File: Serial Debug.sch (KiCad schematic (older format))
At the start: 19 parts, among them J7 USB_OTG, U9 FT230XQ

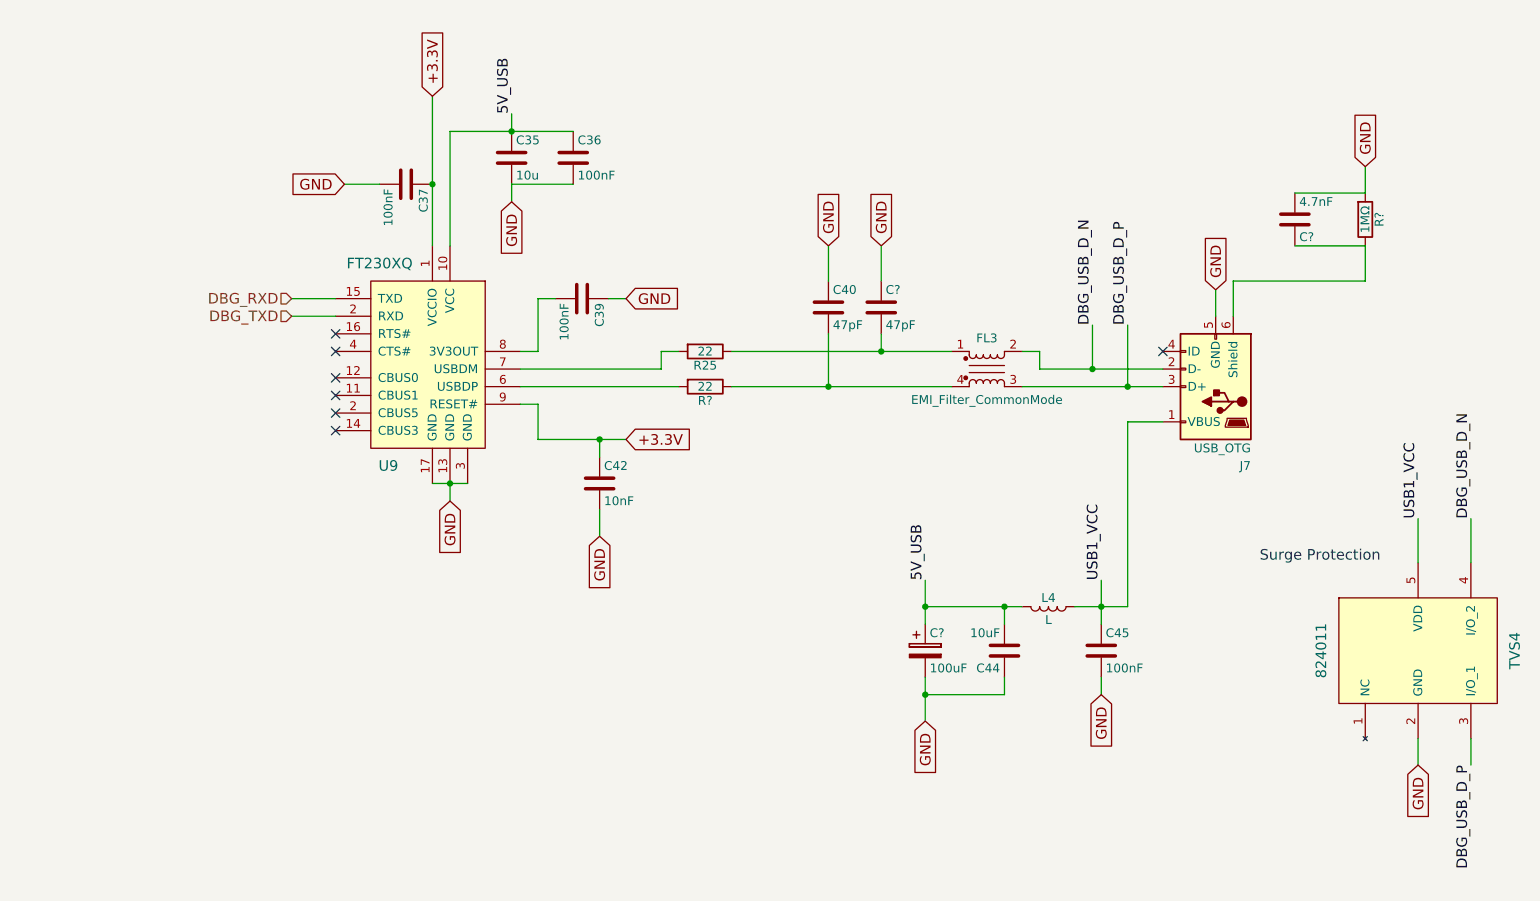
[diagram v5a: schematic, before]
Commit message: part numbers generated;
pcb generation started
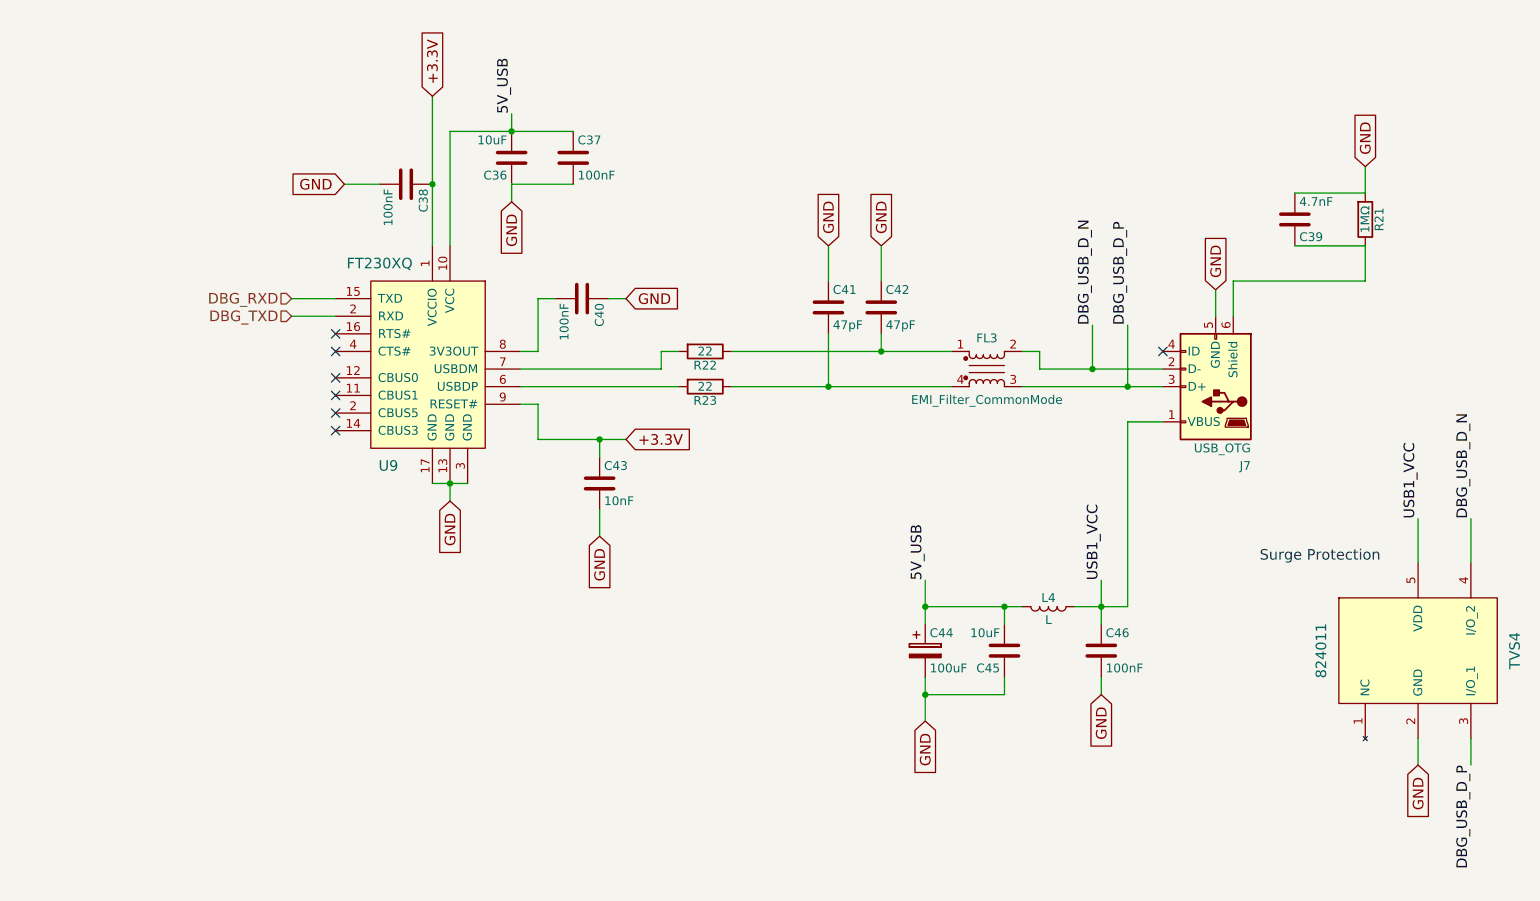
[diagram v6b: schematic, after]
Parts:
- removed C35: 10u, symbol C
- added C36: 10uF, Capacitors_SMD:C_0603_HandSoldering, symbol C
- gave numbers to parts that had none: 5
- renumbered C36 to C37, C37 to C38, C39 to C40, C40 to C41, C42 to C43, C44 to C45, C45 to C46, R25 to R22
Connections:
- net 5V_USB: now also C36.2
- net GND: now also C36.1
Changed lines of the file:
@@
 	3200 3450 3200 3650
 $Comp
-L R R25
+L R R22
 U 1 1 59A2A431
 P 4150 3150
-F 0 "R25" V 4230 3150 50  0000 C CNN
+F 0 "R22" V 4230 3150 50  0000 C CNN
 F 1 "22" V 4150 3150 50  0000 C CNN
 F 2 "Resistors_SMD:R_0603_HandSoldering" V 4080 3150 50  0001 C CNN
@@
 GND
 $Comp
-L C C40
+L C C41
 U 1 1 59A2FC88
 P 4850 2900
-F 0 "C40" H 4875 3000 50  0000 L CNN
+F 0 "C41" H 4875 3000 50  0000 L CNN
 F 1 "47pF" H 4875 2800 50  0000 L CNN
 F 2 "Capacitors_SMD:C_0603_HandSoldering" H 4888 2750 50  0001 C CNN
@@
 Text Label 3050 1800 1    60   ~ 0
 5V_USB
-$Comp
-L C C35
-U 1 1 59A63DF8
-P 3050 2050
-F 0 "C35" H 3075 2150 50  0000 L CNN
-F 1 "10u" H 3075 1950 50  0000 L CNN
-F 2 "" H 3088 1900 50  0001 C CNN
-F 3 "" H 3050 2050 50  0001 C CNN
-	1    3050 2050
-	1    0    0    -1
-$EndComp
 Text GLabel 3050 2300 3    60   Input ~ 0
 GND
@@
 	3900 3150 4000 3150
 $Comp
-L C C44
+L C C45
 U 1 1 59A86400
 P 5850 4850
-F 0 "C44" H 5875 4950 50  0000 L CNN
+F 0 "C45" H 5875 4950 50  0000 L CNN
 F 1 "10uF" H 5875 4750 50  0000 L CNN
 F 2 "Capacitors_SMD:C_0603_HandSoldering" H 5888 4700 30  0001 C CNN
@@
 Connection ~ 5850 4600
 $Comp
-L C C42
+L C C43
 U 1 1 59A67671
 P 3550 3900
-F 0 "C42" H 3575 4000 50  0000 L CNN
+F 0 "C43" H 3575 4000 50  0000 L CNN
 F 1 "10nF" H 3575 3800 50  0000 L CNN
 F 2 "Capacitors_SMD:C_0603_HandSoldering" H 3588 3750 50  0001 C CNN
@@
 $EndComp
 $Comp
-L C C39
+L C C40
 U 1 1 59A67F9E
 P 3450 2850
-F 0 "C39" H 3475 2950 50  0000 L CNN
+F 0 "C40" H 3475 2950 50  0000 L CNN
 F 1 "100nF" H 3475 2750 50  0000 L CNN
 F 2 "Capacitors_SMD:C_0603_HandSoldering" H 3488 2700 30  0001 C CNN
@@
 $EndComp
 $Comp
-L C C45
+L C C46
 U 1 1 59A68788
 P 6400 4850
-F 0 "C45" H 6425 4950 50  0000 L CNN
+F 0 "C46" H 6425 4950 50  0000 L CNN
 F 1 "100nF" H 6425 4750 50  0000 L CNN
 F 2 "Capacitors_SMD:C_0603_HandSoldering" H 6438 4700 30  0001 C CNN
@@
 $EndComp
 $Comp
-L C C36
+L C C37
 U 1 1 59A68F5E
 P 3400 2050
-F 0 "C36" H 3425 2150 50  0000 L CNN
+F 0 "C37" H 3425 2150 50  0000 L CNN
 F 1 "100nF" H 3425 1950 50  0000 L CNN
 F 2 "Capacitors_SMD:C_0603_HandSoldering" H 3438 1900 30  0001 C CNN
@@
 $EndComp
 $Comp
-L C C37
+L C C38
 U 1 1 59A69729
 P 2450 2200
-F 0 "C37" H 2475 2300 50  0000 L CNN
+F 0 "C38" H 2475 2300 50  0000 L CNN
 F 1 "100nF" H 2475 2100 50  0000 L CNN
 F 2 "Capacitors_SMD:C_0603_HandSoldering" H 2488 2050 30  0001 C CNN
@@
 $EndComp
 $Comp
-L R R?
+L R R21
 U 1 1 59AA0F3A
 P 7900 2400
-F 0 "R?" V 7980 2400 50  0000 C CNN
+F 0 "R21" V 7980 2400 50  0000 C CNN
 F 1 "1MΩ" V 7900 2400 50  0000 C CNN
 F 2 "Resistors_SMD:R_0603_HandSoldering" V 7830 2400 50  0001 C CNN
@@
 $EndComp
 $Comp
-L C C?
+L C C39
 U 1 1 59AA0F41
 P 7500 2400
-F 0 "C?" H 7525 2500 50  0000 L CNN
+F 0 "C39" H 7525 2500 50  0000 L CNN
 F 1 "4.7nF" H 7525 2300 50  0000 L CNN
 F 2 "Capacitors_SMD:C_0603_HandSoldering" H 7538 2250 50  0001 C CNN
@@
 	7900 2250 7900 2100
 $Comp
-L R R?
+L R R23
 U 1 1 59A9B327
 P 4150 3350
-F 0 "R?" V 4230 3350 50  0000 C CNN
+F 0 "R23" V 4230 3350 50  0000 C CNN
 F 1 "22" V 4150 3350 50  0000 C CNN
 F 2 "Resistors_SMD:R_0603_HandSoldering" V 4080 3350 50  0001 C CNN
@@
 $EndComp
 $Comp
-L C C?
+L C C42
 U 1 1 59A9B888
 P 5150 2900
-F 0 "C?" H 5175 3000 50  0000 L CNN
+F 0 "C42" H 5175 3000 50  0000 L CNN
 F 1 "47pF" H 5175 2800 50  0000 L CNN
 F 2 "Capacitors_SMD:C_0603_HandSoldering" H 5188 2750 50  0001 C CNN
@@
 $EndComp
 $Comp
-L CP C?
+L CP C44
 U 1 1 59AA48F7
 P 5400 4850
-F 0 "C?" H 5425 4950 50  0000 L CNN
+F 0 "C44" H 5425 4950 50  0000 L CNN
 F 1 "100uF" H 5425 4750 50  0000 L CNN
 F 2 "Capacitors_SMD:CP_Elec_6.3x5.7" H 5438 4700 50  0001 C CNN
@@
 	1    0    0    -1
 $EndComp
+$Comp
+L C C36
+U 1 1 59AB9266
+P 3050 2050
+F 0 "C36" H 3075 2150 50  0000 L CNN
+F 1 "10uF" H 3075 1950 50  0000 L CNN
+F 2 "Capacitors_SMD:C_0603_HandSoldering" H 3088 1900 30  0001 C CNN
+F 3 "http://hu.farnell.com/murata/grm188r60g106me47d/cap-mlcc-x5r-10uf-4v-0603/dp/2688517" H 3050 2050 60  0001 C CNN
+F 4 "http://hu.farnell.com/avx/06036d106mat2a/cap-mlcc-x5r-10uf-6-3v-0603/dp/1833804" H 3050 2050 60  0001 C CNN "avx"
+	1    3050 2050
+	-1   0    0    1
+$EndComp
 $EndSCHEMATC

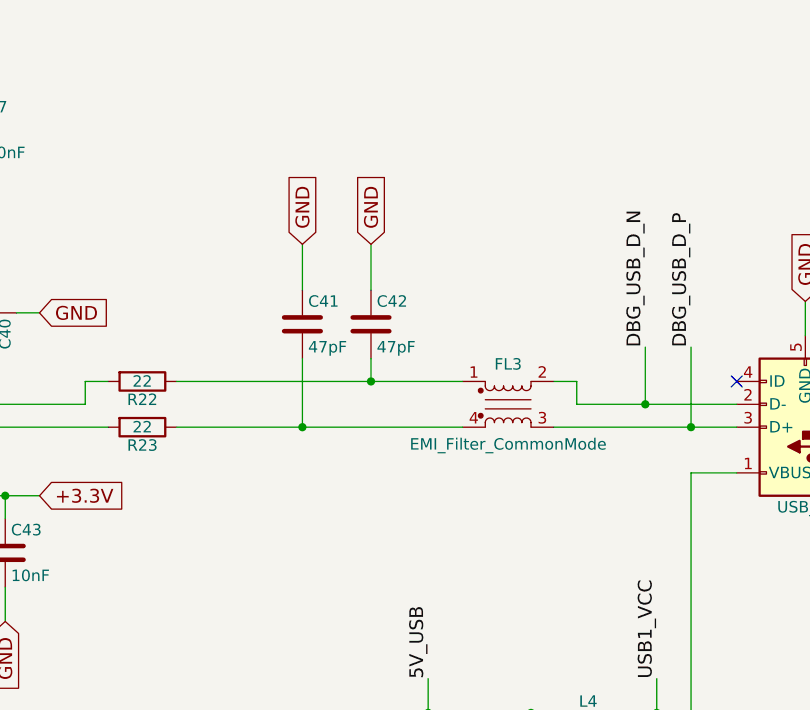
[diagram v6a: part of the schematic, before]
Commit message: I have replaced the normal usb, with a vertical usb.
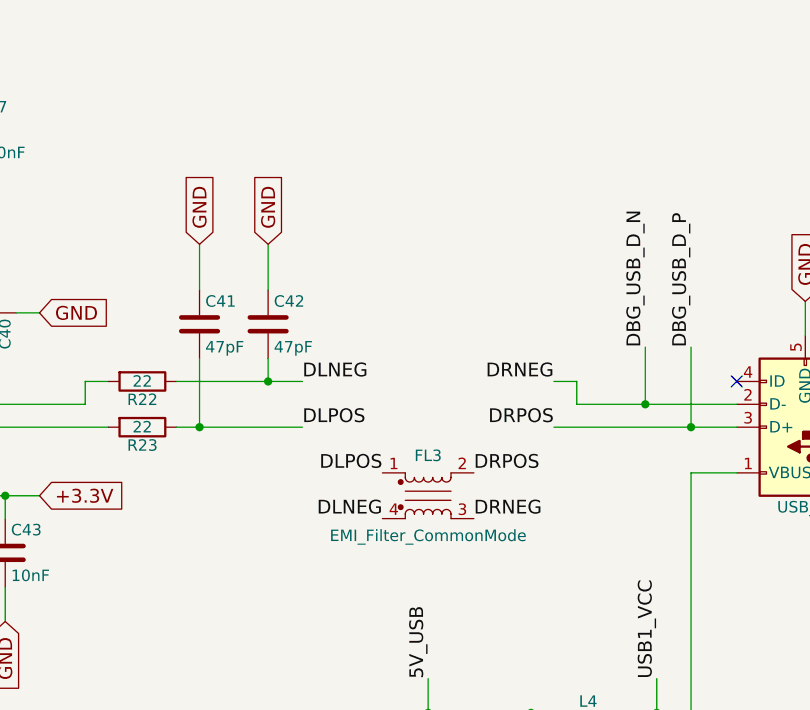
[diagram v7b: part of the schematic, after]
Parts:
- J7: footprint Connectors_USB:USB_Micro-B_Molex-105017-0001 -> Connectors_USB_Complete:USB_Micro-B_Vertical_Molex-105133-0001
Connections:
- net DBG_USB_D_N: now also FL3.3; no longer FL3.2
- net DBG_USB_D_P: now also FL3.2; no longer FL3.3
- net DLNEG: now reaches C42.2, R22.1
- net DLNEG: now also FL3.4; no longer FL3.1
- net DLPOS: now reaches C41.2, R23.1
- net DLPOS: now also FL3.1; no longer FL3.4
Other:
- moved on the sheet: C41, C42, FL3
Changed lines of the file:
@@
 Text GLabel 3700 2850 2    60   Input ~ 0
 GND
-Wire Wire Line
-	3700 2850 3600 2850
-Wire Wire Line
-	2800 3900 2600 3900
-Connection ~ 2700 3900
 Text GLabel 2700 4000 3    60   Input ~ 0
 GND
-Wire Wire Line
-	2700 3900 2700 4000
 NoConn ~ 2050 3600
 NoConn ~ 2050 3500
@@
 Text HLabel 1800 2950 0    60   Input ~ 0
 DBG_TXD
-Wire Wire Line
-	1800 2850 2050 2850
-Wire Wire Line
-	1800 2950 2050 2950
-Wire Wire Line
-	3300 2850 3200 2850
-Wire Wire Line
-	3200 2850 3200 3150
-Wire Wire Line
-	3200 3150 3100 3150
 Text GLabel 3700 3650 2    60   Input ~ 0
 +3.3V
 Text GLabel 3550 4200 3    60   Input ~ 0
 GND
-Wire Wire Line
-	3550 4200 3550 4050
-Wire Wire Line
-	3200 3650 3700 3650
-Wire Wire Line
-	3550 3750 3550 3650
-Connection ~ 3550 3650
-Wire Wire Line
-	3100 3450 3200 3450
-Wire Wire Line
-	3200 3450 3200 3650
 $Comp
 L R R22
@@
 L EMI_Filter_CommonMode FL3
 U 1 1 59A2AADC
-P 5750 3250
-F 0 "FL3" H 5750 3425 50  0000 C CNN
-F 1 "EMI_Filter_CommonMode" H 5750 3075 50  0000 C CNN
-F 2 "water:744233121" V 5750 3290 50  0001 C CNN
-F 3 "http://hu.farnell.com/wurth-elektronik/744233121/line-filter-lvds-0805-120ohm-0/dp/1848957" V 5750 3290 50  0001 C CNN
-	1    5750 3250
-	1    0    0    -1
-$EndComp
-Wire Wire Line
-	4000 3350 3100 3350
-Wire Wire Line
-	4300 3350 5550 3350
-Wire Wire Line
-	4300 3150 5550 3150
-Wire Wire Line
-	3100 3250 3900 3250
+P 5400 3650
+F 0 "FL3" H 5400 3825 50  0000 C CNN
+F 1 "EMI_Filter_CommonMode" H 5400 3475 50  0000 C CNN
+F 2 "water:744233121" V 5400 3690 50  0001 C CNN
+F 3 "http://hu.farnell.com/wurth-elektronik/744233121/line-filter-lvds-0805-120ohm-0/dp/1848957" V 5400 3690 50  0001 C CNN
+	1    5400 3650
+	1    0    0    -1
+$EndComp
 $Comp
 L USB_OTG J7
@@
 F 0 "J7" H 6850 3800 50  0000 L CNN
 F 1 "USB_OTG" H 6850 3700 50  0000 L CNN
-F 2 "Connectors_USB:USB_Micro-B_Molex-105017-0001" H 7200 3300 50  0001 C CNN
-F 3 "http://hu.farnell.com/hirose-hrs/zx62d-b-5pa8-30/micro-usb-2-0-type-b-rcpt-smt/dp/2554981" H 7200 3300 50  0001 C CNN
+F 2 "Connectors_USB_Complete:USB_Micro-B_Vertical_Molex-105133-0001" H 7200 3300 50  0001 C CNN
+F 3 "http://hu.farnell.com/molex/105133-0001/micro-usb-2-0-type-b-receptacle/dp/2751682" H 7200 3300 50  0001 C CNN
 	1    7050 3350
 	-1   0    0    1
@@
 Text GLabel 7900 2100 1    60   Input ~ 0
 GND
-Wire Wire Line
-	7900 2750 7150 2750
-Wire Wire Line
-	7150 2750 7150 2950
-Wire Wire Line
-	7050 2800 7050 2950
 NoConn ~ 6750 3150
 $Comp
@@
 	0    1    1    0
 $EndComp
-Wire Wire Line
-	5400 4450 5400 4700
-Wire Wire Line
-	5400 4600 5950 4600
-Wire Wire Line
-	6400 4450 6400 4700
-Wire Wire Line
-	6250 4600 6550 4600
-Wire Wire Line
-	5400 5000 5400 5250
-Wire Wire Line
-	5400 5100 5850 5100
 Text GLabel 6400 5100 3    60   Input ~ 0
 GND
-Wire Wire Line
-	6400 5100 6400 5000
 Text GLabel 5400 5250 3    60   Input ~ 0
 GND
-Connection ~ 5400 5100
 Text Label 5400 4450 1    60   ~ 0
 5V_USB
-Connection ~ 5400 4600
 Text Label 6400 4450 1    60   ~ 0
 USB1_VCC
-Connection ~ 6400 4600
-Wire Wire Line
-	6550 4600 6550 3550
-Wire Wire Line
-	6550 3550 6750 3550
-Wire Wire Line
-	5950 3350 6750 3350
-Wire Wire Line
-	5950 3150 6050 3150
-Wire Wire Line
-	6050 3150 6050 3250
-Wire Wire Line
-	6050 3250 6750 3250
-Text GLabel 4850 2550 1    60   Input ~ 0
-GND
-Text GLabel 5150 2550 1    60   Input ~ 0
+Text GLabel 4400 2550 1    60   Input ~ 0
+GND
+Text GLabel 4700 2550 1    60   Input ~ 0
 GND
 $Comp
 L C C41
 U 1 1 59A2FC88
-P 4850 2900
-F 0 "C41" H 4875 3000 50  0000 L CNN
-F 1 "47pF" H 4875 2800 50  0000 L CNN
-F 2 "Capacitors_SMD:C_0603_HandSoldering" H 4888 2750 50  0001 C CNN
-F 3 "http://hu.farnell.com/avx/06035a470jat2a/cap-mlcc-c0g-np0-47pf-50v-0603/dp/498567" H 4850 2900 50  0001 C CNN
-	1    4850 2900
-	1    0    0    -1
-$EndComp
-Wire Wire Line
-	5150 2550 5150 2750
-Wire Wire Line
-	4850 2550 4850 2750
-Wire Wire Line
-	5150 3050 5150 3150
-Connection ~ 5150 3150
-Wire Wire Line
-	4850 3050 4850 3350
-Connection ~ 4850 3350
+P 4400 2900
+F 0 "C41" H 4425 3000 50  0000 L CNN
+F 1 "47pF" H 4425 2800 50  0000 L CNN
+F 2 "Capacitors_SMD:C_0603_HandSoldering" H 4438 2750 50  0001 C CNN
+F 3 "http://hu.farnell.com/avx/06035a470jat2a/cap-mlcc-c0g-np0-47pf-50v-0603/dp/498567" H 4400 2900 50  0001 C CNN
+	1    4400 2900
+	1    0    0    -1
+$EndComp
 $Comp
 L 824011 TVS4
@@
 Text GLabel 8200 5500 3    60   Input ~ 0
 GND
-Wire Wire Line
-	8200 5500 8200 5350
 Text Label 8200 4100 1    60   ~ 0
 USB1_VCC
-Wire Wire Line
-	8200 4100 8200 4350
 Text Label 6350 3000 1    60   ~ 0
 DBG_USB_D_N
 Text Label 6550 3000 1    60   ~ 0
 DBG_USB_D_P
-Wire Wire Line
-	6550 3000 6550 3350
-Connection ~ 6550 3350
-Wire Wire Line
-	6350 3000 6350 3250
-Connection ~ 6350 3250
 Text Label 8500 5500 3    60   ~ 0
 DBG_USB_D_P
 Text Label 8500 4100 1    60   ~ 0
 DBG_USB_D_N
-Wire Wire Line
-	8500 4100 8500 4350
-Wire Wire Line
-	8500 5350 8500 5500
 Text Label 3050 1800 1    60   ~ 0
 5V_USB
 Text GLabel 3050 2300 3    60   Input ~ 0
 GND
-Wire Wire Line
-	3050 2200 3050 2300
-Wire Wire Line
-	3050 2200 3400 2200
-Wire Wire Line
-	2700 1900 3400 1900
-Wire Wire Line
-	3050 1900 3050 1800
-Wire Wire Line
-	2700 1900 2700 2550
-Connection ~ 3050 1900
 Text GLabel 2600 1700 1    60   Input ~ 0
 +3.3V
-Wire Wire Line
-	2600 1700 2600 2550
-Wire Wire Line
-	2300 2200 2100 2200
-Connection ~ 2600 2200
 Text GLabel 2100 2200 0    60   Input ~ 0
 GND
-Wire Wire Line
-	3900 3250 3900 3150
-Wire Wire Line
-	3900 3150 4000 3150
 $Comp
 L C C45
@@
 	-1   0    0    1
 $EndComp
-Wire Wire Line
-	5850 5100 5850 5000
-Wire Wire Line
-	5850 4700 5850 4600
-Connection ~ 5850 4600
 $Comp
 L C C43
@@
 	1    0    0    1
 $EndComp
-Wire Wire Line
-	7900 2750 7900 2550
-Wire Wire Line
-	7900 2550 7500 2550
-Wire Wire Line
-	7500 2250 7900 2250
-Wire Wire Line
-	7900 2250 7900 2100
 $Comp
 L R R23
@@
 L C C42
 U 1 1 59A9B888
-P 5150 2900
-F 0 "C42" H 5175 3000 50  0000 L CNN
-F 1 "47pF" H 5175 2800 50  0000 L CNN
-F 2 "Capacitors_SMD:C_0603_HandSoldering" H 5188 2750 50  0001 C CNN
-F 3 "http://hu.farnell.com/avx/06035a470jat2a/cap-mlcc-c0g-np0-47pf-50v-0603/dp/498567" H 5150 2900 50  0001 C CNN
-	1    5150 2900
+P 4700 2900
+F 0 "C42" H 4725 3000 50  0000 L CNN
+F 1 "47pF" H 4725 2800 50  0000 L CNN
+F 2 "Capacitors_SMD:C_0603_HandSoldering" H 4738 2750 50  0001 C CNN
+F 3 "http://hu.farnell.com/avx/06035a470jat2a/cap-mlcc-c0g-np0-47pf-50v-0603/dp/498567" H 4700 2900 50  0001 C CNN
+	1    4700 2900
 	1    0    0    -1
 $EndComp
@@
 	-1   0    0    1
 $EndComp
+Wire Wire Line
+	3700 2850 3600 2850
+Wire Wire Line
+	2800 3900 2600 3900
+Connection ~ 2700 3900
+Wire Wire Line
+	2700 3900 2700 4000
+Wire Wire Line
+	1800 2850 2050 2850
+Wire Wire Line
+	1800 2950 2050 2950
+Wire Wire Line
+	3300 2850 3200 2850
+Wire Wire Line
+	3200 2850 3200 3150
+Wire Wire Line
+	3200 3150 3100 3150
+Wire Wire Line
+	3550 4200 3550 4050
+Wire Wire Line
+	3200 3650 3700 3650
+Wire Wire Line
+	3550 3750 3550 3650
+Connection ~ 3550 3650
+Wire Wire Line
+	3100 3450 3200 3450
+Wire Wire Line
+	3200 3450 3200 3650
+Wire Wire Line
+	4000 3350 3100 3350
+Wire Wire Line
+	3100 3250 3900 3250
+Wire Wire Line
+	7900 2750 7150 2750
+Wire Wire Line
+	7150 2750 7150 2950
+Wire Wire Line
+	7050 2800 7050 2950
+Wire Wire Line
+	5400 4450 5400 4700
+Wire Wire Line
+	5400 4600 5950 4600
+Wire Wire Line
+	6400 4450 6400 4700
+Wire Wire Line
+	6250 4600 6550 4600
+Wire Wire Line
+	5400 5000 5400 5250
+Wire Wire Line
+	5400 5100 5850 5100
+Wire Wire Line
+	6400 5100 6400 5000
+Connection ~ 5400 5100
+Connection ~ 5400 4600
+Connection ~ 6400 4600
+Wire Wire Line
+	6550 4600 6550 3550
+Wire Wire Line
+	6550 3550 6750 3550
+Wire Wire Line
+	5950 3350 6750 3350
+Wire Wire Line
+	5950 3150 6050 3150
+Wire Wire Line
+	6050 3150 6050 3250
+Wire Wire Line
+	6050 3250 6750 3250
+Wire Wire Line
+	4700 2550 4700 2750
+Wire Wire Line
+	4400 2550 4400 2750
+Wire Wire Line
+	4700 3050 4700 3150
+Connection ~ 4700 3150
+Wire Wire Line
+	4400 3050 4400 3350
+Connection ~ 4400 3350
+Wire Wire Line
+	8200 5500 8200 5350
+Wire Wire Line
+	8200 4100 8200 4350
+Wire Wire Line
+	6550 3000 6550 3350
+Connection ~ 6550 3350
+Wire Wire Line
+	6350 3000 6350 3250
+Connection ~ 6350 3250
+Wire Wire Line
+	8500 4100 8500 4350
+Wire Wire Line
+	8500 5350 8500 5500
+Wire Wire Line
+	3050 2200 3050 2300
+Wire Wire Line
+	3050 2200 3400 2200
+Wire Wire Line
+	2700 1900 3400 1900
+Wire Wire Line
+	3050 1900 3050 1800
+Wire Wire Line
+	2700 1900 2700 2550
+Connection ~ 3050 1900
+Wire Wire Line
+	2600 1700 2600 2550
+Wire Wire Line
+	2300 2200 2100 2200
+Connection ~ 2600 2200
+Wire Wire Line
+	3900 3250 3900 3150
+Wire Wire Line
+	3900 3150 4000 3150
+Wire Wire Line
+	5850 5100 5850 5000
+Wire Wire Line
+	5850 4700 5850 4600
+Connection ~ 5850 4600
+Wire Wire Line
+	7900 2750 7900 2550
+Wire Wire Line
+	7900 2550 7500 2550
+Wire Wire Line
+	7500 2250 7900 2250
+Wire Wire Line
+	7900 2250 7900 2100
+Wire Wire Line
+	4300 3150 4850 3150
+Wire Wire Line
+	4300 3350 4850 3350
+Text Label 5600 3550 0    60   ~ 0
+DRPOS
+Text Label 5600 3750 0    60   ~ 0
+DRNEG
+Text Label 5200 3550 2    60   ~ 0
+DLPOS
+Text Label 5200 3750 2    60   ~ 0
+DLNEG
+Text Label 5950 3150 2    60   ~ 0
+DRNEG
+Text Label 5950 3350 2    60   ~ 0
+DRPOS
+Text Label 4850 3350 0    60   ~ 0
+DLPOS
+Text Label 4850 3150 0    60   ~ 0
+DLNEG
 $EndSCHEMATC
